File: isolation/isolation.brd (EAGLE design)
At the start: 74.5 x 72.7 mm, 81 parts, among them IC1 XTLV61048DBVR, IC2 SN74HC14DRG3, IC3 SN74HCS32PWR, IC4 SN74HCS08DYYR, IC5 FDN359BN, IC6 FDN359BN, IC7 FDN359BN, IC8 FDN359BN, J1 S4B-PH-K-S(LF)(SN), J2 S4B-PH-K-S(LF)(SN), J3 S4B-PH-K-S(LF)(SN), J4 S4B-PH-K-S(LF)(SN), J5 S4B-PH-K-S(LF)(SN)

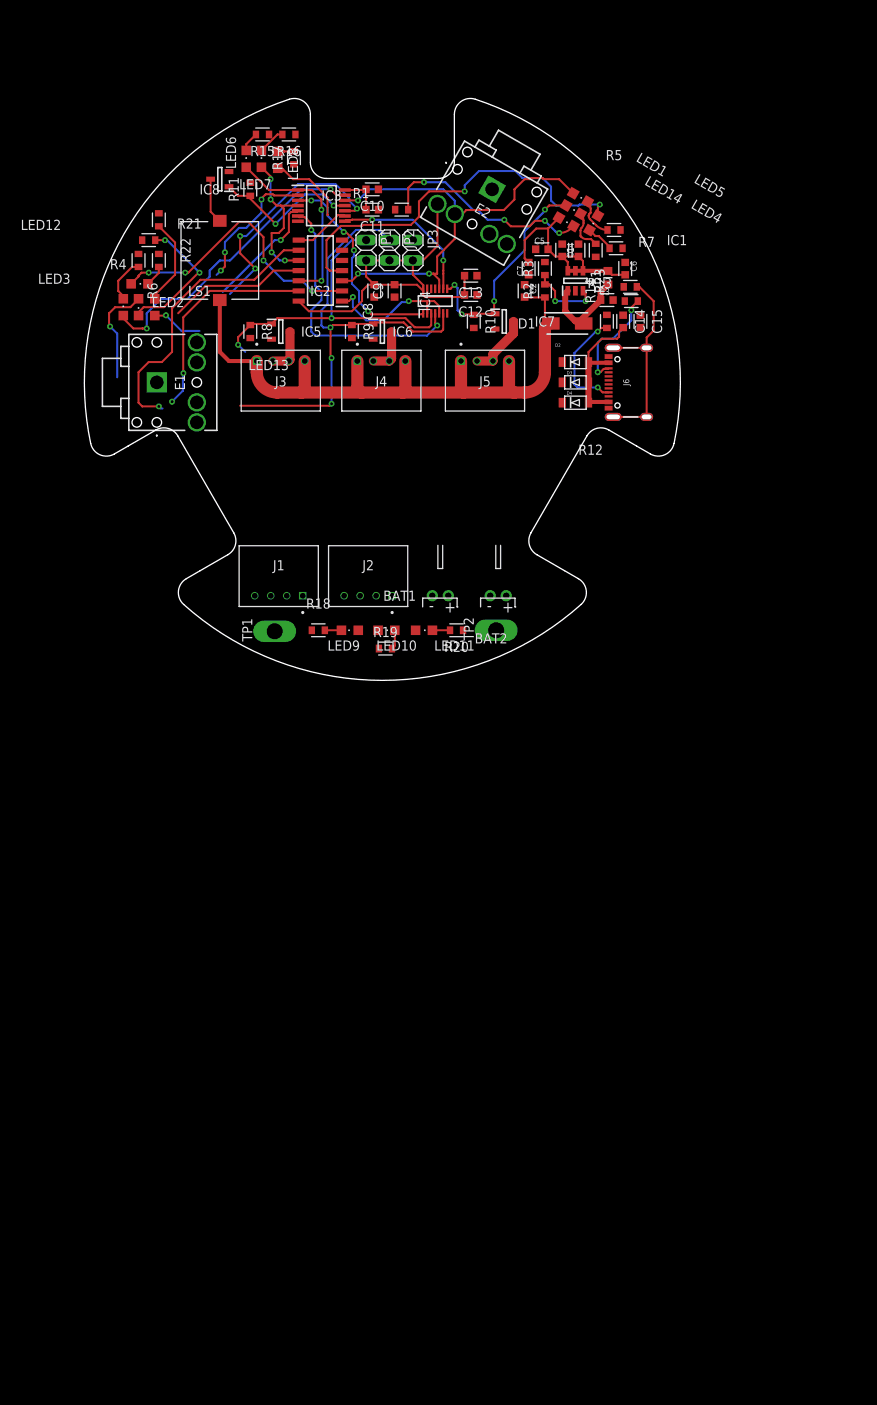
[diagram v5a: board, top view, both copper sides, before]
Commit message: ground and vcc pours
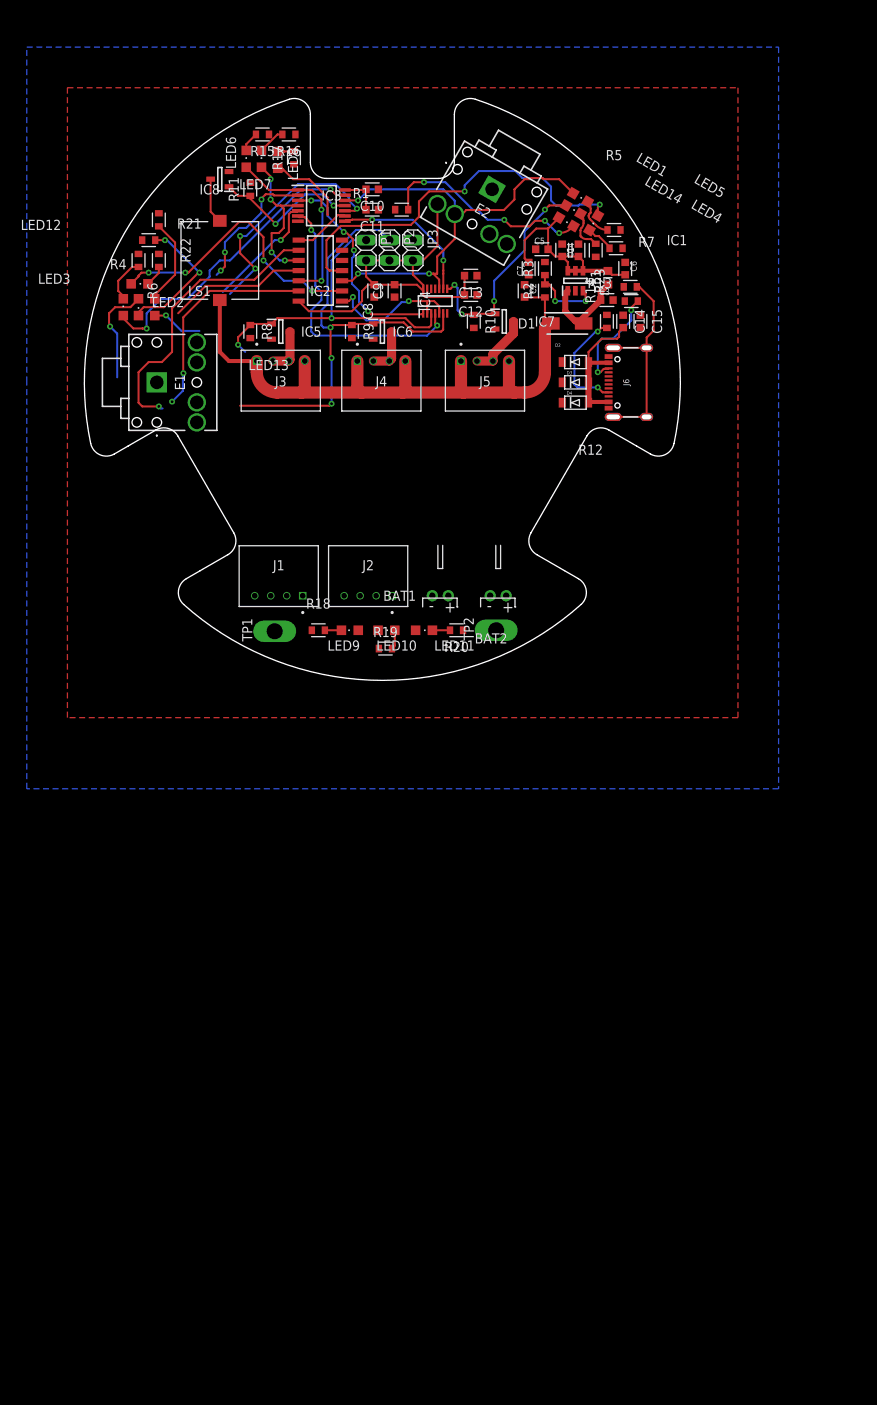
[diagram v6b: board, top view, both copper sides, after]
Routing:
- added copper zone on layer 1, net GND
- added copper zone on layer 16, net VBAT
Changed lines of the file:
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@@
 <contactref element="BAT2" pad="2"/>
 <contactref element="TP1" pad="TP"/>
-<wire x1="-8.8162" y1="-30.988" x2="-13.462" y2="-31.115" width="0" layer="19" extent="1-1"/>
-<wire x1="-9.954" y1="-26.67" x2="-8.8162" y2="-30.988" width="0" layer="19" extent="1-1"/>
-<wire x1="-0.4342" y1="-33.274" x2="-8.8162" y2="-30.988" width="0" layer="19" extent="1-1"/>
-<wire x1="1.222" y1="-26.67" x2="-0.4342" y2="-33.274" width="0" layer="19" extent="1-1"/>
-<wire x1="6.239" y1="-26.67" x2="1.222" y2="-26.67" width="0" layer="19" extent="1-1"/>
-<wire x1="10.0862" y1="-30.988" x2="6.239" y2="-26.67" width="0" layer="19" extent="1-1"/>
-<wire x1="13.478" y1="-26.67" x2="10.0862" y2="-30.988" width="0" layer="19" extent="1-1"/>
-<wire x1="28.28" y1="-3.225" x2="13.478" y2="-26.67" width="0" layer="19" extent="1-1"/>
-<wire x1="28.28" y1="3.225" x2="28.28" y2="-3.225" width="0" layer="19" extent="1-1"/>
-<wire x1="28.067" y1="8.4352" x2="28.28" y2="3.225" width="0" layer="19" extent="1-1"/>
-<wire x1="28.8416" y1="10.287" x2="28.067" y2="8.4352" width="0" layer="19" extent="1-1"/>
-<wire x1="30.2998" y1="10.16" x2="28.8416" y2="10.287" width="0" layer="19" extent="1-1"/>
-<wire x1="30.1728" y1="11.938" x2="30.2998" y2="10.16" width="0" layer="19" extent="1-1"/>
+<polygon width="0.1524" layer="1" isolate="0.254">
+<vertex x="-39.37" y="-41.91"/>
+<vertex x="-39.37" y="36.83"/>
+<vertex x="44.45" y="36.83"/>
+<vertex x="44.45" y="-41.91"/>
+</polygon>
+<wire x1="30.0252" y1="16.764" x2="29.7712" y2="19.05" width="0" layer="19" extent="1-1"/>
+<wire x1="30.353" y1="14.9986" x2="30.0252" y2="16.764" width="0" layer="19" extent="1-1"/>
+<wire x1="30.1728" y1="11.938" x2="30.353" y2="14.9986" width="0" layer="19" extent="1-1"/>
+<wire x1="30.2998" y1="10.16" x2="30.1728" y2="11.938" width="0" layer="19" extent="1-1"/>
+<wire x1="28.8416" y1="10.287" x2="30.2998" y2="10.16" width="0" layer="19" extent="1-1"/>
 <wire x1="30.099" y1="8.3946" x2="30.2998" y2="10.16" width="0" layer="19" extent="1-1"/>
+<wire x1="28.067" y1="8.4352" x2="28.8416" y2="10.287" width="0" layer="19" extent="1-1"/>
 <wire x1="32.258" y1="8.3946" x2="30.099" y2="8.3946" width="0" layer="19" extent="1-1"/>
-<wire x1="30.353" y1="14.9986" x2="30.1728" y2="11.938" width="0" layer="19" extent="1-1"/>
-<wire x1="30.0252" y1="16.764" x2="30.353" y2="14.9986" width="0" layer="19" extent="1-1"/>
-<wire x1="29.7712" y1="19.05" x2="30.0252" y2="16.764" width="0" layer="19" extent="1-1"/>
 <wire x1="26.67" y1="15.6948" x2="30.0252" y2="16.764" width="0" layer="19" extent="1-1"/>
 <wire x1="24.511" y1="17.2846" x2="26.67" y2="15.6948" width="0" layer="19" extent="1-1"/>
@@
 <wire x1="13.3810625" y1="18.549871875" x2="15.546125" y2="17.299871875" width="0" layer="19" extent="1-1"/>
 <wire x1="24.13" y1="11.45" x2="28.8416" y2="10.287" width="0" layer="19" extent="1-1"/>
+<wire x1="28.28" y1="3.225" x2="28.067" y2="8.4352" width="0" layer="19" extent="1-1"/>
 <wire x1="11.8236" y1="13.335" x2="15.546125" y2="17.299871875" width="0" layer="19" extent="1-1"/>
 <wire x1="11.8236" y1="10.922" x2="11.8236" y2="13.335" width="0" layer="19" extent="1-1"/>
@@
 <wire x1="-0.4954" y1="24.13" x2="-0.4954" y2="21.59" width="0" layer="19" extent="1-1"/>
 <wire x1="-10.558" y1="20.148" x2="-5.035" y2="17.78" width="0" layer="19" extent="1-1"/>
+<wire x1="28.28" y1="-3.225" x2="28.28" y2="3.225" width="0" layer="19" extent="1-1"/>
 <wire x1="-11.049" y1="27.2518" x2="-10.558" y2="20.148" width="0" layer="19" extent="1-1"/>
 <wire x1="-10.8688" y1="30.988" x2="-11.049" y2="27.2518" width="0" layer="19" extent="1-1"/>
@@
 <wire x1="-30.48" y1="16.0552" x2="-30.0252" y2="17.78" width="0" layer="19" extent="1-1"/>
 <wire x1="-27.94" y1="16.0552" x2="-30.48" y2="16.0552" width="0" layer="19" extent="1-1"/>
+<wire x1="13.478" y1="-26.67" x2="28.28" y2="-3.225" width="0" layer="19" extent="1-1"/>
+<wire x1="10.0862" y1="-30.988" x2="13.478" y2="-26.67" width="0" layer="19" extent="1-1"/>
+<wire x1="6.239" y1="-26.67" x2="10.0862" y2="-30.988" width="0" layer="19" extent="1-1"/>
+<wire x1="1.222" y1="-26.67" x2="6.239" y2="-26.67" width="0" layer="19" extent="1-1"/>
+<wire x1="-0.4342" y1="-33.274" x2="1.222" y2="-26.67" width="0" layer="19" extent="1-1"/>
+<wire x1="-8.8162" y1="-30.988" x2="-0.4342" y2="-33.274" width="0" layer="19" extent="1-1"/>
+<wire x1="-9.954" y1="-26.67" x2="-8.8162" y2="-30.988" width="0" layer="19" extent="1-1"/>
+<wire x1="-13.462" y1="-31.115" x2="-8.8162" y2="-30.988" width="0" layer="19" extent="1-1"/>
 </signal>
 <signal name="VBAT">
@@
 <wire x1="-1.7654" y1="12.2046" x2="-1.016" y2="12.2046" width="0.254" layer="1"/>
 <contactref element="TP2" pad="TP"/>
-<wire x1="-23.194" y1="-5" x2="14.224" y2="-30.988" width="0" layer="19" extent="1-1"/>
-<wire x1="-10.459" y1="10.16" x2="-23.194" y2="-5" width="0" layer="19" extent="1-1"/>
+<polygon width="0.1524" layer="16" isolate="0.254">
+<vertex x="-44.45" y="0"/>
+<vertex x="-44.45" y="41.91"/>
+<vertex x="49.53" y="41.91"/>
+<vertex x="49.53" y="-50.8"/>
+<vertex x="-44.45" y="-50.8"/>
+</polygon>
+<wire x1="10.2744" y1="13.335" x2="18.288" y2="14.9986" width="0" layer="19" extent="1-1"/>
 <wire x1="-2.0446" y1="21.59" x2="-2.032" y2="15.24" width="0" layer="19" extent="1-1"/>
-<wire x1="18.288" y1="14.9986" x2="10.2744" y2="13.335" width="0" layer="19" extent="1-1"/>
 <wire x1="22.4925" y1="2.54" x2="23.18" y2="13.95" width="0" layer="19" extent="1-1"/>
 <wire x1="22.4925" y1="0" x2="22.4925" y2="2.54" width="0" layer="19" extent="1-1"/>
 <wire x1="22.4925" y1="-2.54" x2="22.4925" y2="0" width="0" layer="19" extent="1-1"/>
+<wire x1="-23.194" y1="-5" x2="-10.459" y2="10.16" width="0" layer="19" extent="1-1"/>
 <wire x1="15.478" y1="-26.67" x2="22.4925" y2="-2.54" width="0" layer="19" extent="1-1"/>
+<wire x1="14.224" y1="-30.988" x2="15.478" y2="-26.67" width="0" layer="19" extent="1-1"/>
 <wire x1="8.239" y1="-26.67" x2="15.478" y2="-26.67" width="0" layer="19" extent="1-1"/>
 </signal>

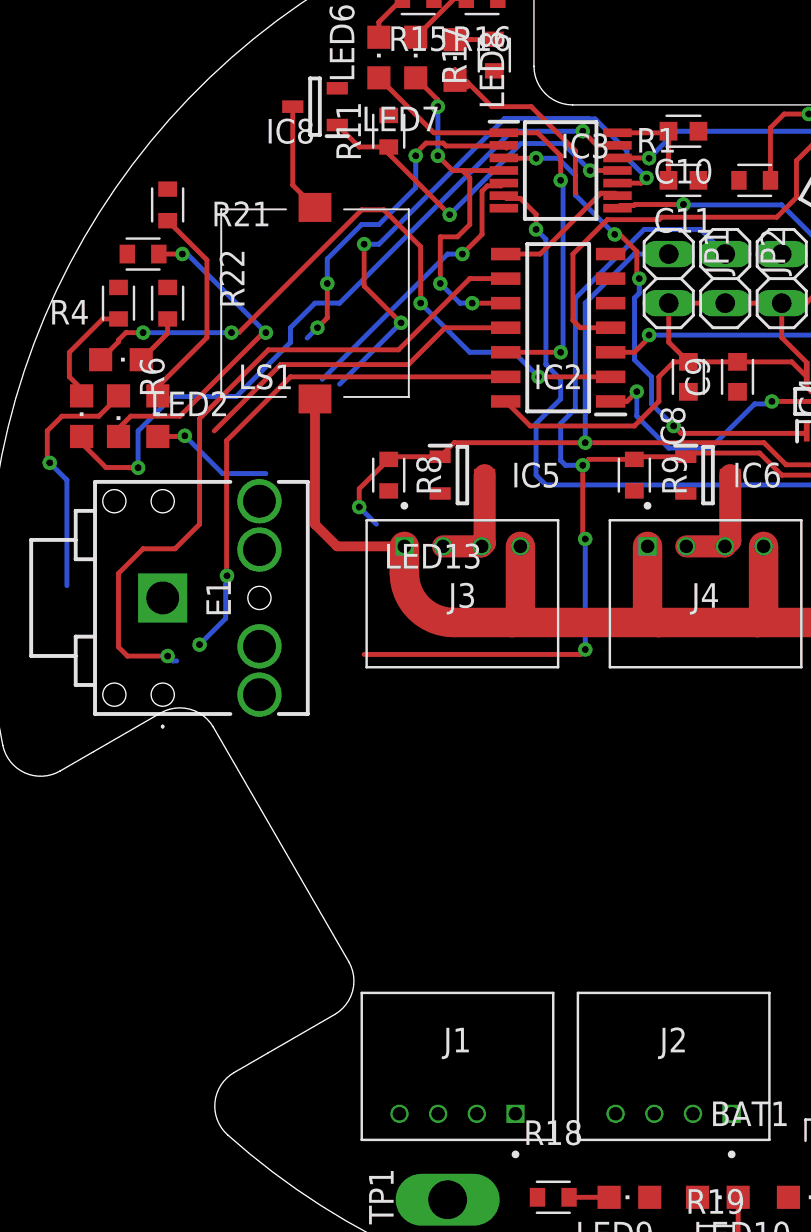
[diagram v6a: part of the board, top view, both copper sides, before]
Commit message: wire lower connectors
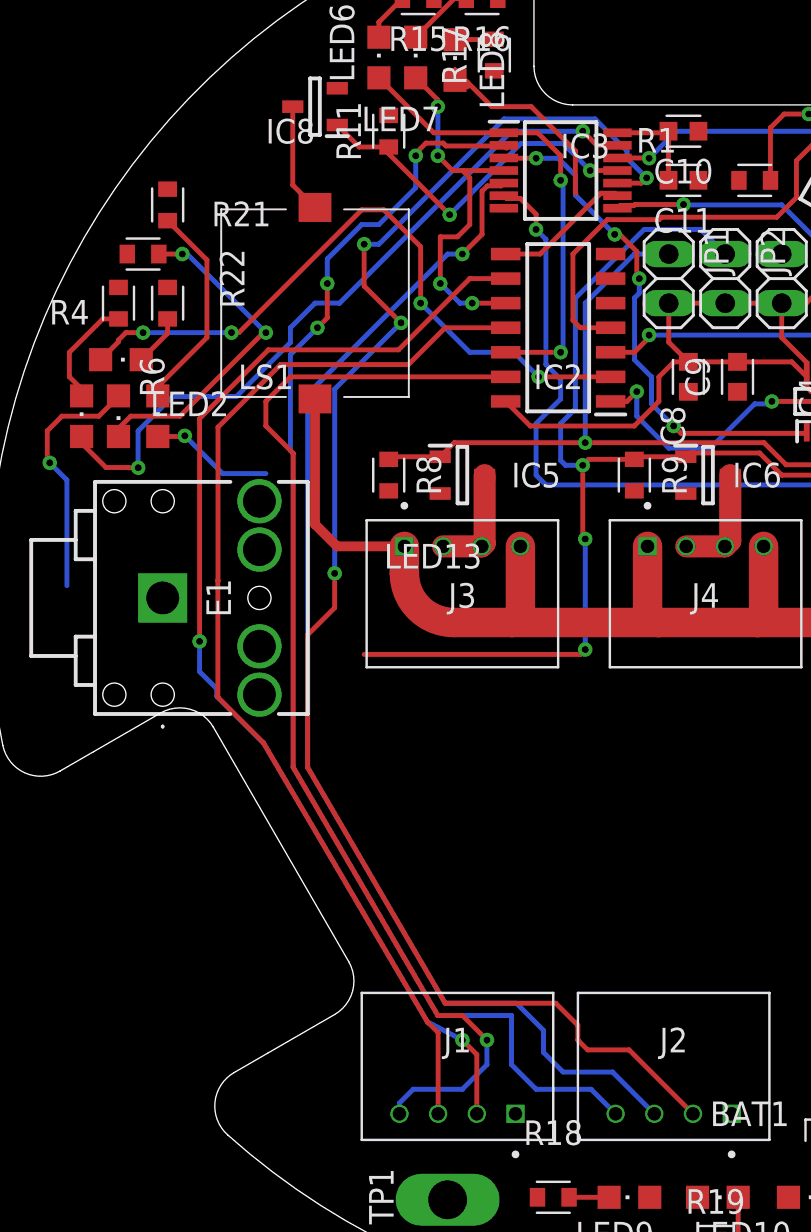
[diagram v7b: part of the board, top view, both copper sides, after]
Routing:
- net PICKLE1: track 17.5 -> 67.7 mm
- net PICKLE3: track 29.8 -> 80.0 mm, vias 3 -> 4
- net PICKLE2: track 14.9 -> 63.2 mm
- net RAVEN2: track 17.3 -> 56.1 mm
- net RAVEN1: track 26.9 -> 57.5 mm, vias 2 -> 1
- net RAVEN3: track 36.6 -> 59.9 mm, vias 1 -> 2
- net FIRE1: track 54.8 -> 50.5 mm, vias 3 -> 2

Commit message: more routing
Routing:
- net FIRE2: track 64.2 -> 117.4 mm, vias 4 -> 10
- net VBAT: track 81.5 -> 117.6 mm, vias 0 -> 3
- net FIRE1: track 50.5 -> 86.2 mm, vias 2 -> 10
- net EN1: track 56.0 -> 87.8 mm, vias 4 -> 6
- net FIRE3: track 28.3 -> 36.1 mm
- net PICKLE3: track 80.0 -> 86.7 mm
- net PICKLE2: track 63.2 -> 68.5 mm
- net PICKLE1: track 67.7 -> 72.8 mm
- net N$26: track 17.3 -> 19.5 mm
- net INVR3: track 18.1 -> 19.1 mm
- net N$2: track 11.1 -> 11.7 mm
